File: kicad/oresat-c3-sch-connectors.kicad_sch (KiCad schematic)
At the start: 29 parts, among them J1 J-SAMTEC-TFM-120-01-L-D-RA, J2 J-TE-Debug-2-1734592-0, J3 J-MOLEX-SMPM-73300-003X, J4 J-MOLEX-SMPM-73300-003X

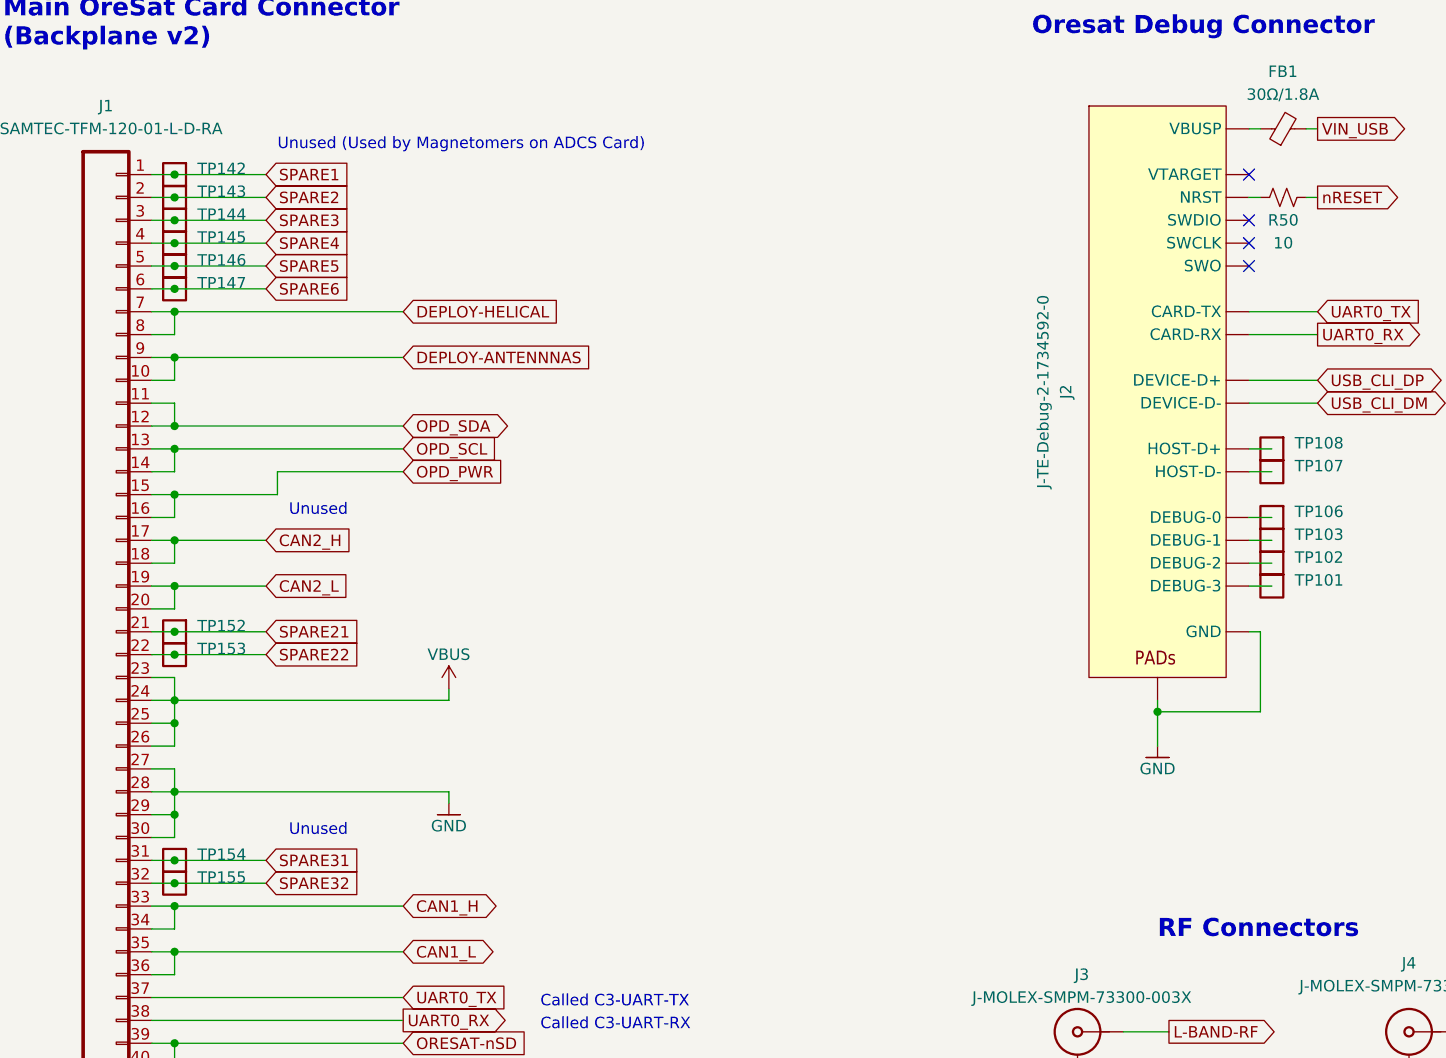
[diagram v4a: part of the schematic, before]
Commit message: Sane amount of ERC errors now; mostly library cleanups.
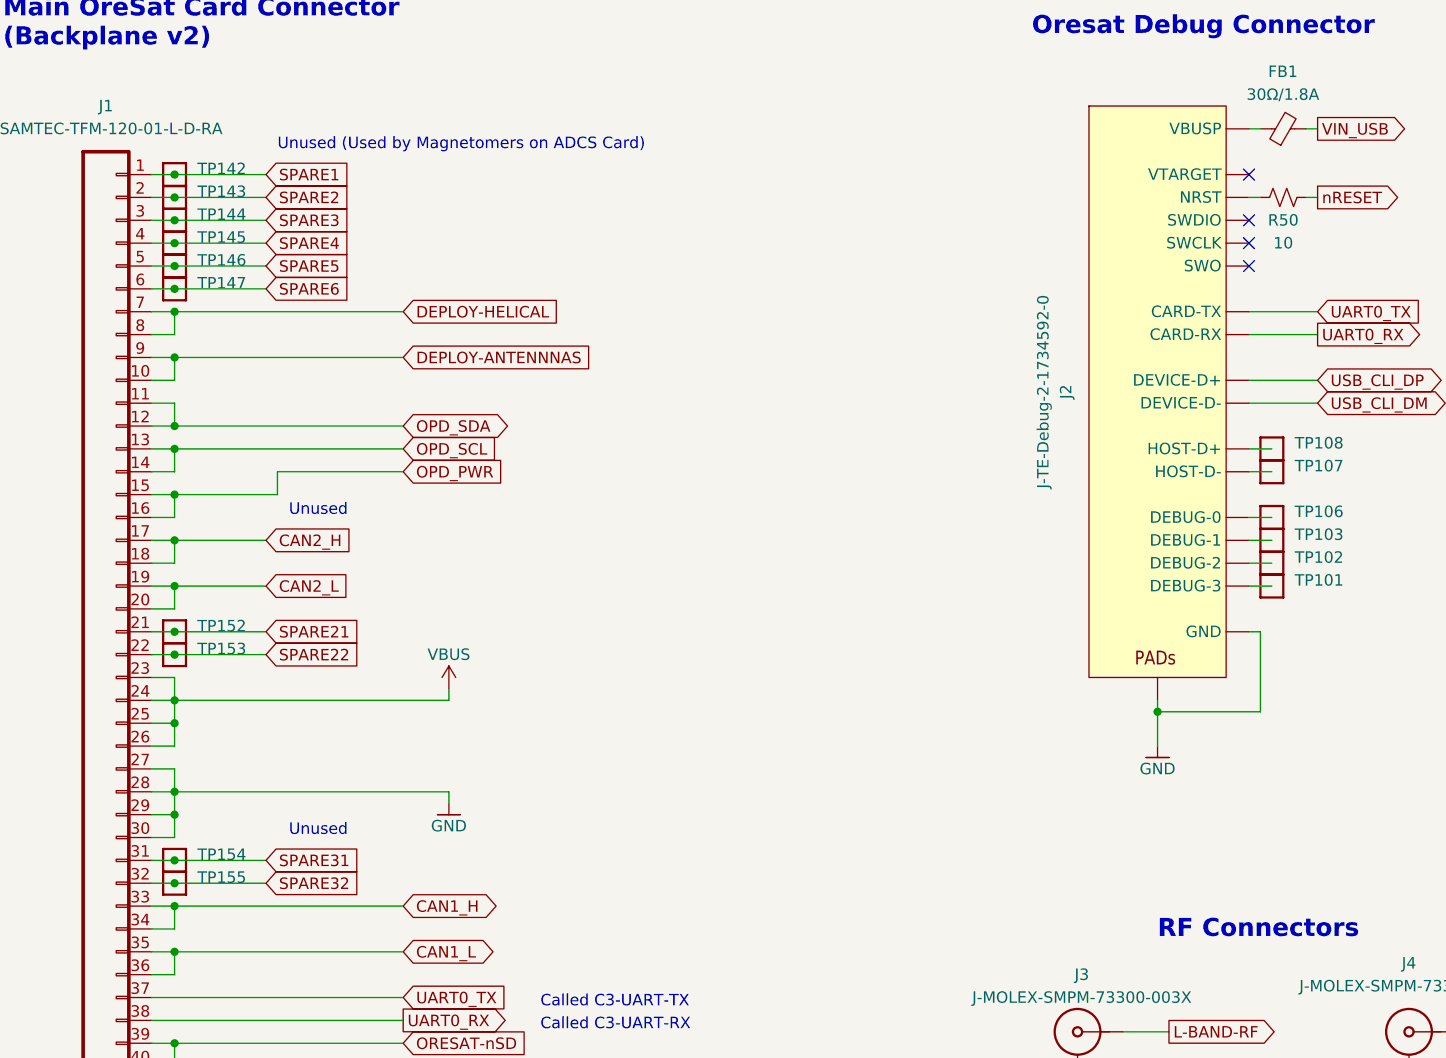
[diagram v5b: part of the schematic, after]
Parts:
- TP101, TP102, TP103, TP106, TP107, TP108, TP142, TP143, TP144, TP145, TP146, TP147, TP152, TP153, TP154, TP155: footprint OreSat-TestPoint:PAD.03X.04 -> oresat-misc:PAD.03X.04; symbol OreSat-TestPoint:Test-Point -> oresat-misc:Test-Point
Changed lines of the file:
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@@
     )
   )
-  (symbol (lib_id "OreSat-TestPoint:Test-Point") (at 91.44 93.98 270) (unit 1)
+  (symbol (lib_id "oresat-misc:Test-Point") (at 91.44 93.98 270) (unit 1)
     (in_bom yes) (on_board yes) (dnp no)
     (property "Reference" "TP147" (at 93.98 93.345 90)
@@
       (effects (font (size 1.27 1.27)) hide)
     )
-    (property "Footprint" "OreSat-TestPoint:PAD.03X.04" (at 93.98 93.98 0)
+    (property "Footprint" "oresat-misc:PAD.03X.04" (at 93.98 93.98 0)
       (effects (font (size 1.27 1.27)) hide)
     )
@@
     )
   )
-  (symbol (lib_id "OreSat-TestPoint:Test-Point") (at 91.44 88.9 270) (unit 1)
+  (symbol (lib_id "oresat-misc:Test-Point") (at 91.44 88.9 270) (unit 1)
     (in_bom yes) (on_board yes) (dnp no)
     (property "Reference" "TP145" (at 93.98 88.265 90)
@@
       (effects (font (size 1.27 1.27)) hide)
     )
-    (property "Footprint" "OreSat-TestPoint:PAD.03X.04" (at 93.98 88.9 0)
+    (property "Footprint" "oresat-misc:PAD.03X.04" (at 93.98 88.9 0)
       (effects (font (size 1.27 1.27)) hide)
     )
@@
     )
   )
-  (symbol (lib_id "OreSat-TestPoint:Test-Point") (at 91.44 86.36 270) (unit 1)
+  (symbol (lib_id "oresat-misc:Test-Point") (at 91.44 86.36 270) (unit 1)
     (in_bom yes) (on_board yes) (dnp no)
     (property "Reference" "TP144" (at 93.98 85.725 90)
@@
       (effects (font (size 1.27 1.27)) hide)
     )
-    (property "Footprint" "OreSat-TestPoint:PAD.03X.04" (at 93.98 86.36 0)
+    (property "Footprint" "oresat-misc:PAD.03X.04" (at 93.98 86.36 0)
       (effects (font (size 1.27 1.27)) hide)
     )
@@
     )
   )
-  (symbol (lib_id "OreSat-TestPoint:Test-Point") (at 91.44 83.82 270) (unit 1)
+  (symbol (lib_id "oresat-misc:Test-Point") (at 91.44 83.82 270) (unit 1)
     (in_bom yes) (on_board yes) (dnp no)
     (property "Reference" "TP143" (at 93.98 83.185 90)
@@
       (effects (font (size 1.27 1.27)) hide)
     )
-    (property "Footprint" "OreSat-TestPoint:PAD.03X.04" (at 93.98 83.82 0)
+    (property "Footprint" "oresat-misc:PAD.03X.04" (at 93.98 83.82 0)
       (effects (font (size 1.27 1.27)) hide)
     )
@@
     )
   )
-  (symbol (lib_id "OreSat-TestPoint:Test-Point") (at 213.36 124.46 270) (unit 1)
+  (symbol (lib_id "oresat-misc:Test-Point") (at 213.36 124.46 270) (unit 1)
     (in_bom yes) (on_board yes) (dnp no)
     (property "Reference" "TP102" (at 215.9 123.825 90)
@@
       (effects (font (size 1.27 1.27)) hide)
     )
-    (property "Footprint" "OreSat-TestPoint:PAD.03X.04" (at 215.9 124.46 0)
+    (property "Footprint" "oresat-misc:PAD.03X.04" (at 215.9 124.46 0)
       (effects (font (size 1.27 1.27)) hide)
     )
@@
     )
   )
-  (symbol (lib_id "OreSat-TestPoint:Test-Point") (at 213.36 114.3 270) (unit 1)
+  (symbol (lib_id "oresat-misc:Test-Point") (at 213.36 114.3 270) (unit 1)
     (in_bom yes) (on_board yes) (dnp no)
     (property "Reference" "TP107" (at 215.9 113.665 90)
@@
       (effects (font (size 1.27 1.27)) hide)
     )
-    (property "Footprint" "OreSat-TestPoint:PAD.03X.04" (at 215.9 114.3 0)
+    (property "Footprint" "oresat-misc:PAD.03X.04" (at 215.9 114.3 0)
       (effects (font (size 1.27 1.27)) hide)
     )
@@
     )
   )
-  (symbol (lib_id "OreSat-TestPoint:Test-Point") (at 213.36 121.92 270) (unit 1)
+  (symbol (lib_id "oresat-misc:Test-Point") (at 213.36 121.92 270) (unit 1)
     (in_bom yes) (on_board yes) (dnp no)
     (property "Reference" "TP103" (at 215.9 121.285 90)
@@
       (effects (font (size 1.27 1.27)) hide)
     )
-    (property "Footprint" "OreSat-TestPoint:PAD.03X.04" (at 215.9 121.92 0)
+    (property "Footprint" "oresat-misc:PAD.03X.04" (at 215.9 121.92 0)
       (effects (font (size 1.27 1.27)) hide)
     )
@@
     )
   )
-  (symbol (lib_id "OreSat-TestPoint:Test-Point") (at 213.36 119.38 270) (unit 1)
+  (symbol (lib_id "oresat-misc:Test-Point") (at 213.36 119.38 270) (unit 1)
     (in_bom yes) (on_board yes) (dnp no)
     (property "Reference" "TP106" (at 215.9 118.745 90)
@@
       (effects (font (size 1.27 1.27)) hide)
     )
-    (property "Footprint" "OreSat-TestPoint:PAD.03X.04" (at 215.9 119.38 0)
+    (property "Footprint" "oresat-misc:PAD.03X.04" (at 215.9 119.38 0)
       (effects (font (size 1.27 1.27)) hide)
     )
@@
     )
   )
-  (symbol (lib_id "OreSat-TestPoint:Test-Point") (at 91.44 157.48 270) (unit 1)
+  (symbol (lib_id "oresat-misc:Test-Point") (at 91.44 157.48 270) (unit 1)
     (in_bom yes) (on_board yes) (dnp no)
     (property "Reference" "TP154" (at 93.98 156.845 90)
@@
       (effects (font (size 1.27 1.27)) hide)
     )
-    (property "Footprint" "OreSat-TestPoint:PAD.03X.04" (at 93.98 157.48 0)
+    (property "Footprint" "oresat-misc:PAD.03X.04" (at 93.98 157.48 0)
       (effects (font (size 1.27 1.27)) hide)
     )
@@
     )
   )
-  (symbol (lib_id "OreSat-TestPoint:Test-Point") (at 91.44 91.44 270) (unit 1)
+  (symbol (lib_id "oresat-misc:Test-Point") (at 91.44 91.44 270) (unit 1)
     (in_bom yes) (on_board yes) (dnp no)
     (property "Reference" "TP146" (at 93.98 90.805 90)
@@
       (effects (font (size 1.27 1.27)) hide)
     )
-    (property "Footprint" "OreSat-TestPoint:PAD.03X.04" (at 93.98 91.44 0)
+    (property "Footprint" "oresat-misc:PAD.03X.04" (at 93.98 91.44 0)
       (effects (font (size 1.27 1.27)) hide)
     )
@@
     )
   )
-  (symbol (lib_id "OreSat-Power:GND") (at 121.92 151.13 0) (unit 1)
+  (symbol (lib_id "oresat-power:GND") (at 121.92 151.13 0) (unit 1)
     (in_bom yes) (on_board yes) (dnp no)
     (property "Reference" "#GND020" (at 121.92 157.48 0)
@@
     )
   )
-  (symbol (lib_id "OreSat-TestPoint:Test-Point") (at 91.44 134.62 270) (unit 1)
+  (symbol (lib_id "oresat-misc:Test-Point") (at 91.44 134.62 270) (unit 1)
     (in_bom yes) (on_board yes) (dnp no)
     (property "Reference" "TP153" (at 93.98 133.985 90)
@@
       (effects (font (size 1.27 1.27)) hide)
     )
-    (property "Footprint" "OreSat-TestPoint:PAD.03X.04" (at 93.98 134.62 0)
+    (property "Footprint" "oresat-misc:PAD.03X.04" (at 93.98 134.62 0)
       (effects (font (size 1.27 1.27)) hide)
     )
@@
     )
   )
-  (symbol (lib_id "OreSat-Power:GND") (at 200.66 144.78 0) (unit 1)
+  (symbol (lib_id "oresat-power:GND") (at 200.66 144.78 0) (unit 1)
     (in_bom yes) (on_board yes) (dnp no)
     (property "Reference" "#GND0101" (at 200.66 151.13 0)
@@
     )
   )
-  (symbol (lib_id "OreSat-Power:GND") (at 191.77 184.15 0) (unit 1)
+  (symbol (lib_id "oresat-power:GND") (at 191.77 184.15 0) (unit 1)
     (in_bom yes) (on_board yes) (dnp no)
     (property "Reference" "#GND0102" (at 191.77 190.5 0)
@@
     )
   )
-  (symbol (lib_id "OreSat-TestPoint:Test-Point") (at 91.44 81.28 270) (unit 1)
+  (symbol (lib_id "oresat-misc:Test-Point") (at 91.44 81.28 270) (unit 1)
     (in_bom yes) (on_board yes) (dnp no)
     (property "Reference" "TP142" (at 93.98 80.645 90)
@@
       (effects (font (size 1.27 1.27)) hide)
     )
-    (property "Footprint" "OreSat-TestPoint:PAD.03X.04" (at 93.98 81.28 0)
+    (property "Footprint" "oresat-misc:PAD.03X.04" (at 93.98 81.28 0)
       (effects (font (size 1.27 1.27)) hide)
     )
@@
     )
   )
-  (symbol (lib_id "OreSat-TestPoint:Test-Point") (at 91.44 132.08 270) (unit 1)
+  (symbol (lib_id "oresat-misc:Test-Point") (at 91.44 132.08 270) (unit 1)
     (in_bom yes) (on_board yes) (dnp no)
     (property "Reference" "TP152" (at 93.98 131.445 90)
@@
       (effects (font (size 1.27 1.27)) hide)
     )
-    (property "Footprint" "OreSat-TestPoint:PAD.03X.04" (at 93.98 132.08 0)
+    (property "Footprint" "oresat-misc:PAD.03X.04" (at 93.98 132.08 0)
       (effects (font (size 1.27 1.27)) hide)
     )
@@
     )
   )
-  (symbol (lib_id "OreSat-TestPoint:Test-Point") (at 91.44 160.02 270) (unit 1)
+  (symbol (lib_id "oresat-misc:Test-Point") (at 91.44 160.02 270) (unit 1)
     (in_bom yes) (on_board yes) (dnp no)
     (property "Reference" "TP155" (at 93.98 159.385 90)
@@
       (effects (font (size 1.27 1.27)) hide)
     )
-    (property "Footprint" "OreSat-TestPoint:PAD.03X.04" (at 93.98 160.02 0)
-      (effects (font (size 1.27 1.27)) hide)
-    )
-    (property "Datasheet" "" (at 93.98 160.02 0)
+    (property "Footprint" "oresat-misc:PAD.03X.04" (at 91.44 160.02 0)
+      (effects (font (size 1.27 1.27)) hide)
+    )
+    (property "Datasheet" "" (at 91.44 160.02 0)
       (effects (font (size 1.27 1.27)) hide)
     )
@@
     )
   )
-  (symbol (lib_id "OreSat-TestPoint:Test-Point") (at 213.36 111.76 270) (unit 1)
+  (symbol (lib_id "oresat-misc:Test-Point") (at 213.36 111.76 270) (unit 1)
     (in_bom yes) (on_board yes) (dnp no)
     (property "Reference" "TP108" (at 215.9 111.125 90)
@@
       (effects (font (size 1.27 1.27)) hide)
     )
-    (property "Footprint" "OreSat-TestPoint:PAD.03X.04" (at 215.9 111.76 0)
+    (property "Footprint" "oresat-misc:PAD.03X.04" (at 215.9 111.76 0)
       (effects (font (size 1.27 1.27)) hide)
     )
@@
     )
   )
-  (symbol (lib_id "OreSat-Power:GND") (at 228.6 184.15 0) (unit 1)
+  (symbol (lib_id "oresat-power:GND") (at 228.6 184.15 0) (unit 1)
     (in_bom yes) (on_board yes) (dnp no)
     (property "Reference" "#GND017" (at 228.6 190.5 0)
@@
     )
   )
-  (symbol (lib_id "OreSat-TestPoint:Test-Point") (at 213.36 127 270) (unit 1)
+  (symbol (lib_id "oresat-misc:Test-Point") (at 213.36 127 270) (unit 1)
     (in_bom yes) (on_board yes) (dnp no)
     (property "Reference" "TP101" (at 215.9 126.365 90)
@@
       (effects (font (size 1.27 1.27)) hide)
     )
-    (property "Footprint" "OreSat-TestPoint:PAD.03X.04" (at 215.9 127 0)
-      (effects (font (size 1.27 1.27)) hide)
-    )
+    (property "Footprint" "oresat-misc:PAD.03X.04" (at 215.9 127 0)
+      (effects (font (size 1.27 1.27)) hide)
+    )
